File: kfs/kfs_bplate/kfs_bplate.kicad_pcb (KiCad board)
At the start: 2 copper layers, 283 x 93 mm, 9 parts

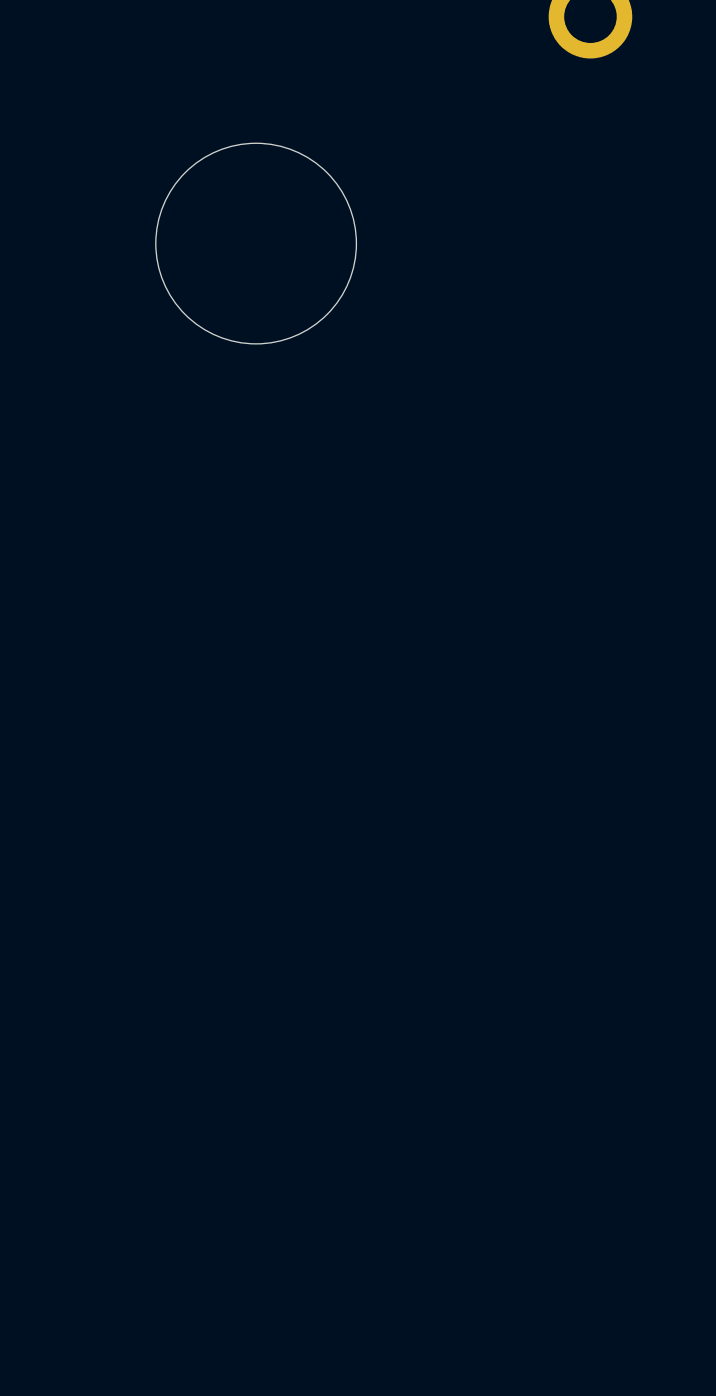
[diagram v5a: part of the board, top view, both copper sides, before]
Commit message: Changed reset button again. Removed some standoffs.
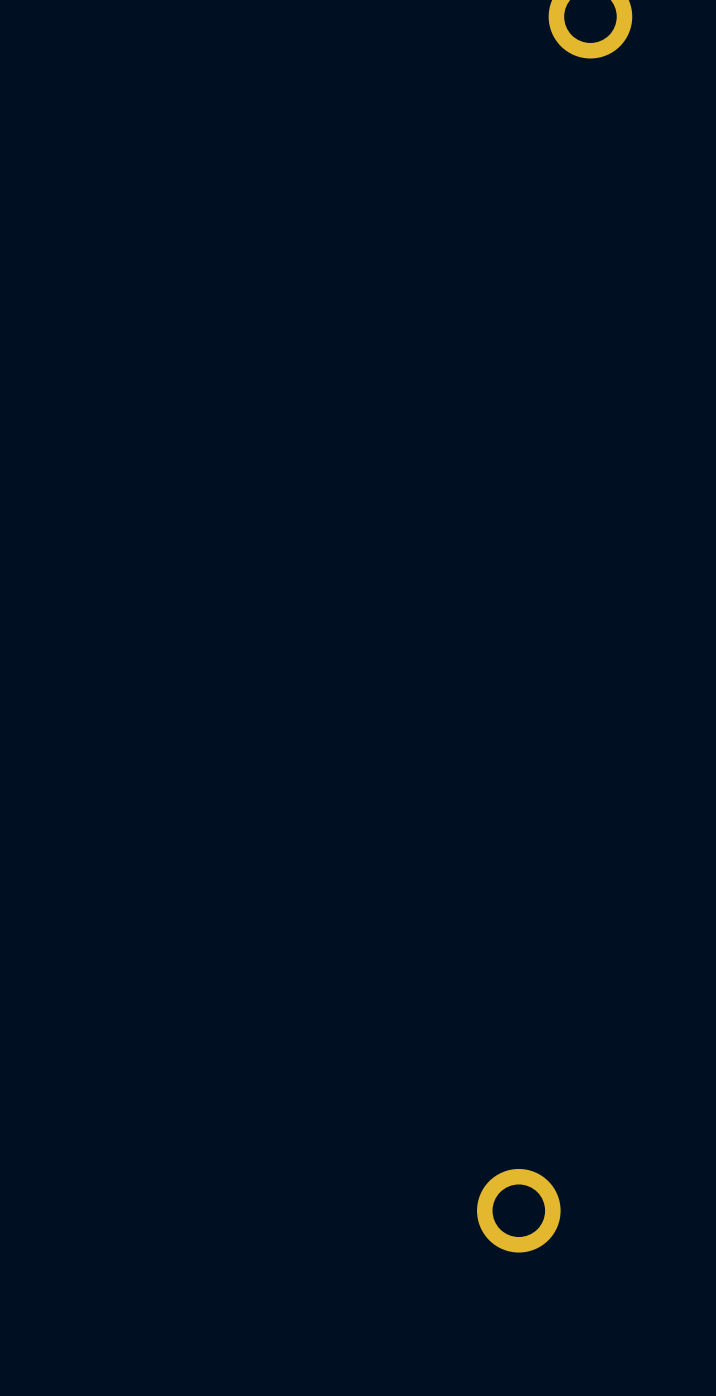
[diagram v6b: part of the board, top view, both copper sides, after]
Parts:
- removed H1: MountingHole, MountingHole:MountingHole_8.4mm_M8
- added H7: MountingHole, MountingHole:MountingHole_2.2mm_M2_ISO7380_Pad, F.Cu at (155.0, 91.5)
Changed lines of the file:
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@@
     (pad "1" thru_hole circle (at 0 0) (size 3.5 3.5) (drill 2.2) (layers "*.Cu" "*.Mask"))
   )
-  (footprint "MountingHole:MountingHole_8.4mm_M8" (layer "F.Cu")
-    (at 144 51)
-    (descr "Mounting Hole 8.4mm, no annular, M8")
-    (tags "mounting hole 8.4mm no annular m8")
+  (footprint "MountingHole:MountingHole_2.2mm_M2_ISO7380_Pad" (layer "F.Cu")
+    (at 155 91.5)
+    (descr "Mounting Hole 2.2mm, M2, ISO7380")
+    (tags "mounting hole 2.2mm m2 iso7380")
     (property "Sheetfile" "kfs_bplate.kicad_sch")
     (property "Sheetname" "")
@@
     (property "ki_keywords" "mounting hole")
     (attr exclude_from_pos_files)
-    (fp_text reference "H1" (at 0 -9.4) (layer "F.SilkS") hide
+    (fp_text reference "H7" (at 0 -2.75) (layer "F.SilkS") hide
         (effects (font (size 1 1) (thickness 0.15)))
     )
-    (fp_text value "MountingHole" (at 0 9.4) (layer "F.Fab")
+    (fp_text value "MountingHole" (at 0 2.75) (layer "F.Fab")
         (effects (font (size 1 1) (thickness 0.15)))
     )
@@
         (effects (font (size 1 1) (thickness 0.15)))
     )
-    (fp_circle (center 0 0) (end 8.4 0)
+    (fp_circle (center 0 0) (end 1.75 0)
       (stroke (width 0.15) (type solid)) (fill none) (layer "Cmts.User"))
-    (fp_circle (center 0 0) (end 8.65 0)
+    (fp_circle (center 0 0) (end 2 0)
       (stroke (width 0.05) (type solid)) (fill none) (layer "F.CrtYd"))
-    (pad "" np_thru_hole circle (at 0 0) (size 8.4 8.4) (drill 8.4) (layers "*.Cu" "*.Mask"))
+    (pad "1" thru_hole circle (at 0 0) (size 3.5 3.5) (drill 2.2) (layers "*.Cu" "*.Mask"))
   )
   (footprint "MountingHole:MountingHole_2.2mm_M2_ISO7380_Pad" (layer "F.Cu")

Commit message: Switched kfs to use nice!nano.
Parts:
- added H1: MountingHole, MountingHole:MountingHole_2.2mm_M2_ISO7380_Pad, F.Cu at (158.6, 84.8)
- added H11: MountingHole, MountingHole:MountingHole_2.2mm_M2_ISO7380_Pad, F.Cu at (290.6, 78.2)
- added H8: MountingHole, MountingHole:MountingHole_2.2mm_M2_ISO7380_Pad, F.Cu at (17.6, 78.2)
- moved H7 24.3 mm to (131.6, 84.8)
- moved H0 6.84 mm to (113.1, 117.8)
- moved H4 6.84 mm to (177.1, 117.8)
- moved H5 6.84 mm to (290.6, 117.8)
- moved H6 6.84 mm to (17.6, 117.8)
- moved H10 3.91 mm to (131.1, 37.8)
- moved H2 3.91 mm to (290.6, 37.8)
- moved H9 3.91 mm to (159.1, 37.8)
- moved H3 3.91 mm to (17.6, 37.8)
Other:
- board size 283 x 93 mm -> 283 x 90 mm

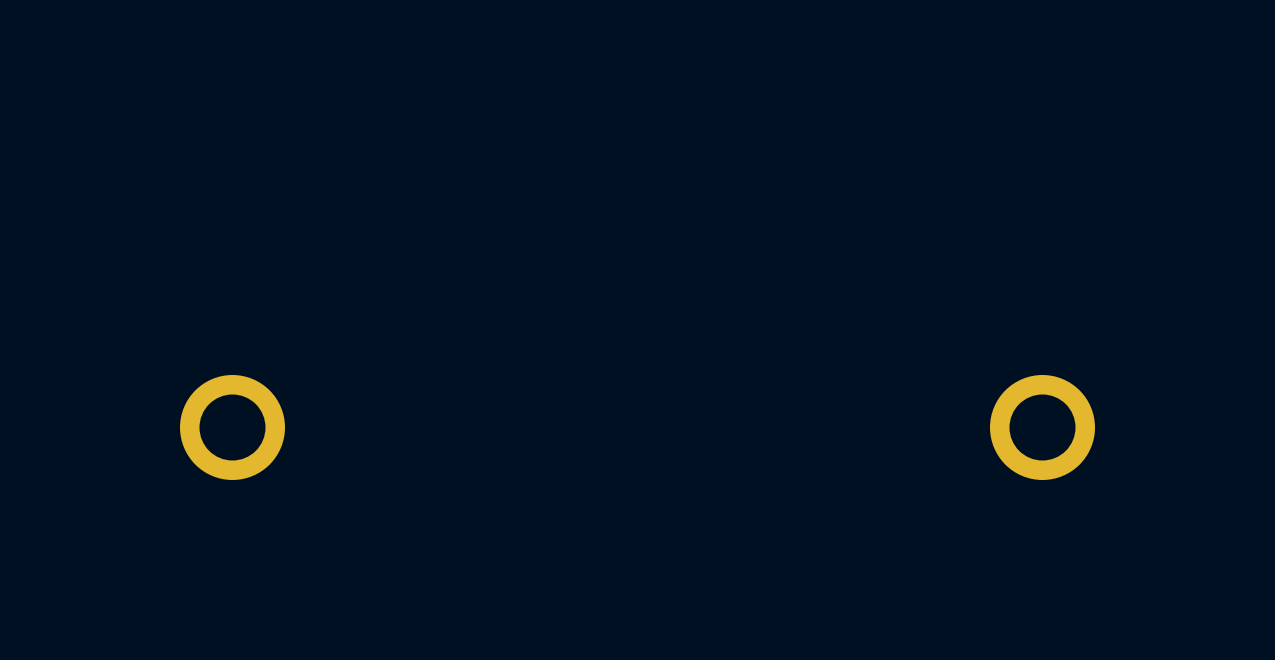
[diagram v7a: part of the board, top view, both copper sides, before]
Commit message: Moved some kfs mounting holes.
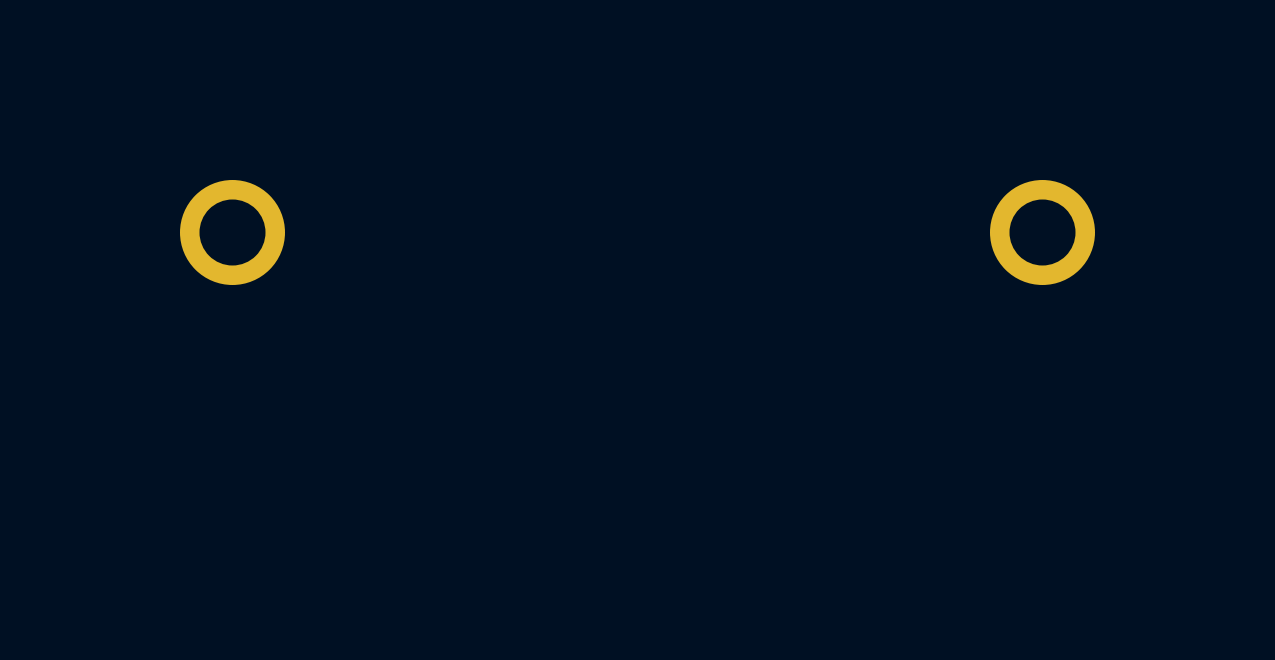
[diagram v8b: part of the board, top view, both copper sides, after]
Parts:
- moved H1 6.50 mm to (158.6, 78.2)
- moved H7 6.50 mm to (131.6, 78.2)
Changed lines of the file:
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@@
   )
   (footprint "MountingHole:MountingHole_2.2mm_M2_ISO7380_Pad" (layer "F.Cu")
-    (at 158.62 84.75)
+    (at 158.62 78.25)
     (descr "Mounting Hole 2.2mm, M2, ISO7380")
     (tags "mounting hole 2.2mm m2 iso7380")
@@
   )
   (footprint "MountingHole:MountingHole_2.2mm_M2_ISO7380_Pad" (layer "F.Cu")
-    (at 131.62 84.75)
+    (at 131.62 78.25)
     (descr "Mounting Hole 2.2mm, M2, ISO7380")
     (tags "mounting hole 2.2mm m2 iso7380")
